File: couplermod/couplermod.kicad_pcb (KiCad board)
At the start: 2 copper layers, 15.2 x 12.7 mm, 6 parts, among them J1 SMA, P1 CONN_2

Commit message: cleanups to coupler mod
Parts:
- moved C2 0.63 mm to (146.3, 103.6)
- moved R1 0.25 mm to (151.1, 102.6)
- moved C1 0.13 mm to (151.1, 106.2)
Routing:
- net Net-(C2-Pad1): track 5.45 -> 6.76 mm
- net Net-(C2-Pad2): track 6.23 -> 6.76 mm
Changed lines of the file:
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@@
     (18 B.Paste user)
     (19 F.Paste user)
-    (20 B.SilkS user)
+    (20 B.SilkS user hide)
     (21 F.SilkS user)
     (22 B.Mask user)
@@
   )
   (module SMD_Packages:SMD-1210 (layer F.Cu)
-    (at 151.13 106.045 180)
+    (at 151.13 106.172 180)
     (tags "CMS SM")
     (attr smd)
-    (fp_text reference C1 (at 3.81 -1.27 180) (layer F.SilkS)
+    (fp_text reference C1 (at 3.556 -0.762 180) (layer F.SilkS)
       (effects (font (size 0.8 0.8) (thickness 0.15)))
     )
@@
   )
   (module SMD_Packages:SMD-1210 (layer F.Cu)
-    (at 146.685 104.14 90)
+    (at 146.304 103.632 90)
     (tags "CMS SM")
     (attr smd)
-    (fp_text reference C2 (at 3.175 -0.635 180) (layer F.SilkS)
+    (fp_text reference C2 (at -3.302 -0.508 180) (layer F.SilkS)
       (effects (font (size 0.8 0.8) (thickness 0.15)))
     )
@@
   (module sma:sma (layer F.Cu)
     (at 141.605 104.775)
-    (fp_text reference J1 (at 4.445 5.08) (layer F.SilkS)
+    (fp_text reference J1 (at 4.191 3.429) (layer F.SilkS)
       (effects (font (size 0.8 0.8) (thickness 0.15)))
     )
@@
     (descr "Connecteurs 2 pins")
     (tags "CONN DEV")
-    (fp_text reference P1 (at 3.81 0.635 180) (layer F.SilkS)
+    (fp_text reference P1 (at 3.556 0 180) (layer F.SilkS)
       (effects (font (size 0.8 0.8) (thickness 0.15)))
     )
@@
   )
   (module SMD_Packages:SMD-1210 (layer F.Cu)
-    (at 151.13 102.87)
+    (at 151.13 102.616)
     (tags "CMS SM")
     (attr smd)
-    (fp_text reference R1 (at 1.905 -2.54) (layer F.SilkS)
+    (fp_text reference R1 (at 1.778 -2.286) (layer F.SilkS)
       (effects (font (size 0.8 0.8) (thickness 0.15)))
     )
@@
     (at 148.59 99.695)
     (attr smd)
-    (fp_text reference R2 (at 2.54 0) (layer F.SilkS)
+    (fp_text reference R2 (at 2.54 -0.127) (layer F.SilkS)
       (effects (font (size 0.8 0.8) (thickness 0.15)))
     )
@@
     )
   )
+  (gr_text couple (at 149.86 103.505 90) (layer B.SilkS)
+    (effects (font (size 1.5 1.5) (thickness 0.3)) (justify mirror))
+  )
   (gr_text gnd (at 152.4 105.41 90) (layer B.SilkS)
-    (effects (font (size 1.5 1.5) (thickness 0.3)) (justify mirror))
-  )
-  (gr_text couple (at 149.86 103.505 90) (layer B.SilkS)
     (effects (font (size 1.5 1.5) (thickness 0.3)) (justify mirror))
   )
@@
   (gr_line (start 154.305 98.425) (end 154.305 111.125) (angle 90) (layer Edge.Cuts) (width 0.1))
   (gr_line (start 141.605 98.425) (end 154.305 98.425) (angle 90) (layer Edge.Cuts) (width 0.1))
-  (segment (start 152.654 106.045) (end 152.654 102.87) (width 1) (layer F.Cu) (net 1))
-  (segment (start 149.606 106.045) (end 149.606 108.966) (width 1) (layer F.Cu) (net 2))
-  (segment (start 149.606 108.966) (end 149.86 109.22) (width 1) (layer F.Cu) (net 2))
-  (segment (start 146.685 105.664) (end 144.399 105.664) (width 1) (layer F.Cu) (net 3))
-  (segment (start 144.399 105.664) (end 143.51 104.775) (width 1) (layer F.Cu) (net 3))
+  (segment (start 152.654 106.172) (end 152.654 102.616) (width 1) (layer F.Cu) (net 1) (status C00000))
+  (segment (start 149.606 106.172) (end 149.606 108.966) (width 1) (layer F.Cu) (net 2) (status C00000))
+  (segment (start 149.606 108.966) (end 149.86 109.22) (width 1) (layer F.Cu) (net 2) (status C00000))
+  (segment (start 146.304 105.156) (end 141.986 105.156) (width 1) (layer F.Cu) (net 3) (status C00000))
+  (segment (start 141.986 105.156) (end 141.605 104.775) (width 1) (layer F.Cu) (net 3) (status C00000))
   (segment (start 143.51 104.775) (end 141.605 104.775) (width 1) (layer F.Cu) (net 3))
-  (segment (start 149.606 102.87) (end 149.606 99.7585) (width 1) (layer F.Cu) (net 4))
-  (segment (start 149.606 99.7585) (end 149.5425 99.695) (width 1) (layer F.Cu) (net 4))
-  (segment (start 146.685 102.616) (end 149.352 102.616) (width 1) (layer F.Cu) (net 4))
-  (segment (start 149.352 102.616) (end 149.606 102.87) (width 1) (layer F.Cu) (net 4))
-  (segment (start 141.605 100.375) (end 144.735 100.375) (width 1) (layer F.Cu) (net 5) (status 400000))
+  (segment (start 149.606 102.616) (end 149.606 102.108) (width 1) (layer F.Cu) (net 4) (status C00000))
+  (segment (start 149.606 102.108) (end 146.304 102.108) (width 1) (layer F.Cu) (net 4) (status C00000))
+  (segment (start 149.5425 99.695) (end 149.5425 102.5525) (width 1) (layer F.Cu) (net 4))
+  (segment (start 149.5425 102.5525) (end 149.606 102.616) (width 1) (layer F.Cu) (net 4))
+  (via (at 146.05 99.695) (size 0.889) (layers F.Cu B.Cu) (net 5))
+  (segment (start 147.6375 99.695) (end 146.05 99.695) (width 1) (layer F.Cu) (net 5))
+  (segment (start 144.735 109.175) (end 144.78 109.22) (width 1) (layer F.Cu) (net 5))
+  (via (at 144.78 109.22) (size 0.889) (layers F.Cu B.Cu) (net 5))
+  (segment (start 141.605 109.175) (end 144.735 109.175) (width 1) (layer F.Cu) (net 5))
+  (segment (start 144.735 100.375) (end 144.78 100.33) (width 1) (layer F.Cu) (net 5))
   (via (at 144.78 100.33) (size 0.889) (layers F.Cu B.Cu) (net 5))
-  (segment (start 144.735 100.375) (end 144.78 100.33) (width 1) (layer F.Cu) (net 5))
-  (segment (start 141.605 109.175) (end 144.735 109.175) (width 1) (layer F.Cu) (net 5))
-  (via (at 144.78 109.22) (size 0.889) (layers F.Cu B.Cu) (net 5))
-  (segment (start 144.735 109.175) (end 144.78 109.22) (width 1) (layer F.Cu) (net 5))
-  (segment (start 147.6375 99.695) (end 146.05 99.695) (width 1) (layer F.Cu) (net 5))
-  (via (at 146.05 99.695) (size 0.889) (layers F.Cu B.Cu) (net 5))
+  (segment (start 141.605 100.375) (end 144.735 100.375) (width 1) (layer F.Cu) (net 5))
   (zone (net 5) (net_name GND) (layer B.Cu) (hatch edge 0.508)
     (connect_pads yes (clearance 0.5))

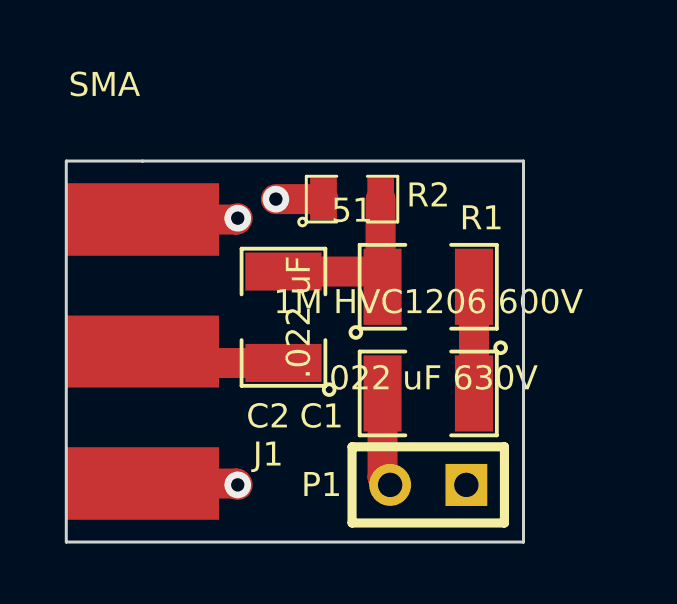
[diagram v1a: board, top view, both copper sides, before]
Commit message: added scripts for using gerbmerge for panelizing boards to reduce assembly costs
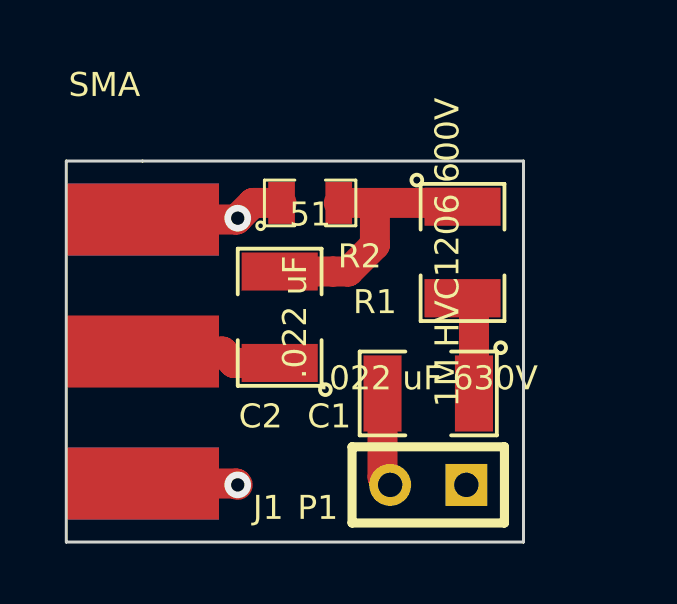
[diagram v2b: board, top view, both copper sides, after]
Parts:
- moved R1 1.62 mm to (152.3, 101.5), turned to 270 degrees
- moved R2 1.40 mm to (147.2, 99.8)
- moved C2 0.13 mm to (146.2, 103.6)
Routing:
- net Net-(C2-Pad2): track 6.76 -> 9.12 mm
- net GND: track 7.97 -> 8.06 mm, vias 3 -> 2
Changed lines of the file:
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@@
     (links 10)
     (no_connects 0)
-    (area 138.801 94.846 157.078049 112.649)
+    (area 138.801 94.846 157.713049 112.649)
     (thickness 1.6)
     (drawings 7)
-    (tracks 18)
+    (tracks 24)
     (zones 0)
     (modules 6)
@@
     (18 B.Paste user)
     (19 F.Paste user)
-    (20 B.SilkS user hide)
+    (20 B.SilkS user)
     (21 F.SilkS user)
     (22 B.Mask user)
@@
   )
   (setup
-    (last_trace_width 1)
+    (last_trace_width 0.254)
     (user_trace_width 1)
     (trace_clearance 0.254)
-    (zone_clearance 0.5)
+    (zone_clearance 1)
     (zone_45_only no)
     (trace_min 0.254)
@@
     (tags "CMS SM")
     (attr smd)
-    (fp_text reference C1 (at 3.556 -0.762 180) (layer F.SilkS)
+    (fp_text reference C1 (at 3.302 -0.762 180) (layer F.SilkS)
       (effects (font (size 0.8 0.8) (thickness 0.15)))
     )
@@
   )
   (module SMD_Packages:SMD-1210 (layer F.Cu)
-    (at 146.304 103.632 90)
+    (at 146.177 103.632 90)
     (tags "CMS SM")
     (attr smd)
-    (fp_text reference C2 (at -3.302 -0.508 180) (layer F.SilkS)
+    (fp_text reference C2 (at -3.302 -0.635 180) (layer F.SilkS)
       (effects (font (size 0.8 0.8) (thickness 0.15)))
     )
@@
   (module sma:sma (layer F.Cu)
     (at 141.605 104.775)
-    (fp_text reference J1 (at 4.191 3.429) (layer F.SilkS)
+    (fp_text reference J1 (at 4.191 5.207) (layer F.SilkS)
       (effects (font (size 0.8 0.8) (thickness 0.15)))
     )
@@
     (descr "Connecteurs 2 pins")
     (tags "CONN DEV")
-    (fp_text reference P1 (at 3.556 0 180) (layer F.SilkS)
+    (fp_text reference P1 (at 3.683 -0.762 180) (layer F.SilkS)
       (effects (font (size 0.8 0.8) (thickness 0.15)))
     )
@@
   )
   (module SMD_Packages:SMD-1210 (layer F.Cu)
-    (at 151.13 102.616)
+    (at 152.273 101.473 270)
     (tags "CMS SM")
     (attr smd)
-    (fp_text reference R1 (at 1.778 -2.286) (layer F.SilkS)
-      (effects (font (size 0.8 0.8) (thickness 0.15)))
-    )
-    (fp_text value "1M HVC1206 600V" (at 0 0.508) (layer F.SilkS)
+    (fp_text reference R1 (at 1.651 2.921 360) (layer F.SilkS)
+      (effects (font (size 0.8 0.8) (thickness 0.15)))
+    )
+    (fp_text value "1M HVC1206 600V" (at 0 0.508 270) (layer F.SilkS)
       (effects (font (size 0.8 0.8) (thickness 0.15)))
     )
@@
     (fp_line (start 2.286 1.397) (end 2.286 -1.397) (layer F.SilkS) (width 0.127))
     (fp_line (start 2.286 -1.397) (end 0.762 -1.397) (layer F.SilkS) (width 0.127))
-    (pad 1 smd rect (at -1.524 0) (size 1.27 2.54) (layers F.Cu F.Paste F.Mask)
+    (pad 1 smd rect (at -1.524 0 270) (size 1.27 2.54) (layers F.Cu F.Paste F.Mask)
       (net 4 "Net-(C2-Pad2)"))
-    (pad 2 smd rect (at 1.524 0) (size 1.27 2.54) (layers F.Cu F.Paste F.Mask)
+    (pad 2 smd rect (at 1.524 0 270) (size 1.27 2.54) (layers F.Cu F.Paste F.Mask)
       (net 1 "Net-(C1-Pad1)"))
     (model smd/chip_cms.wrl
@@
   )
   (module SMD_Packages:SMD-0805 (layer F.Cu)
-    (at 148.59 99.695)
-    (attr smd)
-    (fp_text reference R2 (at 2.54 -0.127) (layer F.SilkS)
+    (at 147.193 99.822)
+    (attr smd)
+    (fp_text reference R2 (at 1.651 1.778) (layer F.SilkS)
       (effects (font (size 0.8 0.8) (thickness 0.15)))
     )
@@
   (gr_line (start 154.305 98.425) (end 154.305 111.125) (angle 90) (layer Edge.Cuts) (width 0.1))
   (gr_line (start 141.605 98.425) (end 154.305 98.425) (angle 90) (layer Edge.Cuts) (width 0.1))
-  (segment (start 152.654 106.172) (end 152.654 102.616) (width 1) (layer F.Cu) (net 1) (status C00000))
-  (segment (start 149.606 106.172) (end 149.606 108.966) (width 1) (layer F.Cu) (net 2) (status C00000))
-  (segment (start 149.606 108.966) (end 149.86 109.22) (width 1) (layer F.Cu) (net 2) (status C00000))
-  (segment (start 146.304 105.156) (end 141.986 105.156) (width 1) (layer F.Cu) (net 3) (status C00000))
-  (segment (start 141.986 105.156) (end 141.605 104.775) (width 1) (layer F.Cu) (net 3) (status C00000))
+  (segment (start 152.654 103.378) (end 152.273 102.997) (width 1) (layer F.Cu) (net 1))
+  (segment (start 152.654 106.172) (end 152.654 103.378) (width 1) (layer F.Cu) (net 1))
+  (segment (start 149.606 106.172) (end 149.606 108.966) (width 1) (layer F.Cu) (net 2))
+  (segment (start 149.606 108.966) (end 149.86 109.22) (width 1) (layer F.Cu) (net 2))
+  (segment (start 141.986 105.156) (end 141.605 104.775) (width 1) (layer F.Cu) (net 3))
   (segment (start 143.51 104.775) (end 141.605 104.775) (width 1) (layer F.Cu) (net 3))
-  (segment (start 149.606 102.616) (end 149.606 102.108) (width 1) (layer F.Cu) (net 4) (status C00000))
-  (segment (start 149.606 102.108) (end 146.304 102.108) (width 1) (layer F.Cu) (net 4) (status C00000))
-  (segment (start 149.5425 99.695) (end 149.5425 102.5525) (width 1) (layer F.Cu) (net 4))
-  (segment (start 149.5425 102.5525) (end 149.606 102.616) (width 1) (layer F.Cu) (net 4))
-  (via (at 146.05 99.695) (size 0.889) (layers F.Cu B.Cu) (net 5))
-  (segment (start 147.6375 99.695) (end 146.05 99.695) (width 1) (layer F.Cu) (net 5))
+  (segment (start 144.272 104.775) (end 144.653 105.156) (width 1) (layer F.Cu) (net 3))
+  (segment (start 144.653 105.156) (end 146.177 105.156) (width 1) (layer F.Cu) (net 3))
+  (segment (start 141.605 104.775) (end 144.272 104.775) (width 1) (layer F.Cu) (net 3))
+  (segment (start 152.146 99.822) (end 152.273 99.949) (width 1) (layer F.Cu) (net 4))
+  (segment (start 149.352 99.822) (end 152.146 99.822) (width 1) (layer F.Cu) (net 4))
+  (segment (start 148.1455 99.822) (end 149.352 99.822) (width 1) (layer F.Cu) (net 4))
+  (segment (start 147.955 102.108) (end 148.463 102.108) (width 1) (layer F.Cu) (net 4))
+  (segment (start 148.463 102.108) (end 149.352 101.219) (width 1) (layer F.Cu) (net 4))
+  (segment (start 149.352 101.219) (end 149.352 99.822) (width 1) (layer F.Cu) (net 4))
+  (segment (start 146.177 102.108) (end 147.955 102.108) (width 1) (layer F.Cu) (net 4))
   (segment (start 144.735 109.175) (end 144.78 109.22) (width 1) (layer F.Cu) (net 5))
   (via (at 144.78 109.22) (size 0.889) (layers F.Cu B.Cu) (net 5))
   (segment (start 141.605 109.175) (end 144.735 109.175) (width 1) (layer F.Cu) (net 5))
+  (segment (start 145.288 99.822) (end 144.78 100.33) (width 1) (layer F.Cu) (net 5))
+  (segment (start 144.735 100.375) (end 141.605 100.375) (width 1) (layer F.Cu) (net 5))
+  (via (at 144.78 100.33) (size 0.889) (layers F.Cu B.Cu) (net 5))
   (segment (start 144.735 100.375) (end 144.78 100.33) (width 1) (layer F.Cu) (net 5))
-  (via (at 144.78 100.33) (size 0.889) (layers F.Cu B.Cu) (net 5))
-  (segment (start 141.605 100.375) (end 144.735 100.375) (width 1) (layer F.Cu) (net 5))
+  (segment (start 146.2405 99.822) (end 145.288 99.822) (width 1) (layer F.Cu) (net 5))
   (zone (net 5) (net_name GND) (layer B.Cu) (hatch edge 0.508)
-    (connect_pads yes (clearance 0.5))
-    (min_thickness 0.5)
+    (connect_pads yes (clearance 1))
+    (min_thickness 1)
     (fill (arc_segments 16) (thermal_gap 5) (thermal_bridge_width 5))
     (polygon
